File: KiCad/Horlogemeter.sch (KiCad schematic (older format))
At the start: 52 parts, among them J1 Serial header, J10 External LED, J2 AVR-ISP-6, J3 Piezo microphone, J4 12v input, J5 Headphones, J6 Gain pot 10k, J7 RTC connector board, J8 I2c display connector, J9 I2c spare, Q1 BC327, U1 ATmega328P-PU, U2 TL072, U3 OPA37GP, U4 L7805, Y1 16Mhz

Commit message: Schema checked, netlist created
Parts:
- removed C11: 10u, Capacitor_THT:CP_Radial_D5.0mm_P2.50mm, symbol Device:CP
- removed C2: 100n, Capacitor_THT:C_Disc_D3.4mm_W2.1mm_P2.50mm, symbol Device:C
- removed R4, R5: 3k3, Resistor_THT:R_Axial_DIN0207_L6.3mm_D2.5mm_P7.62mm_Horizontal, symbol Device:R
- C15: renamed from C17; value 0,01u -> 0,1u
- renumbered C12 to C10, C13 to C11, C14 to C12, C15 to C13, C16 to C14, C18 to C16, C19 to C17, C3 to C2, C4 to C3, C5 to C4, C6 to C5, C7 to C6, C8 to C7, C9 to C8, C10 to C9, J9 to J10, J10 to J8, J8 to J9, R12 to R10, R13 to R11, R14 to R12, R6 to R4, R7 to R5, R8 to R6, R9 to R7, R10 to R8, R11 to R9
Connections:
- net at U1.5 (PD3): now also J7.5 (Pin_5)
- no-connect marks 15 -> 14

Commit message: PCB v1.1 created
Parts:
- J2: footprint Connector_PinSocket_2.54mm:PinSocket_2x03_P2.54mm_Vertical -> Connector_PinHeader_2.54mm:PinHeader_2x03_P2.54mm_Vertical
- J3, J4, J5, J8: footprint (none) -> TerminalBlock:TerminalBlock_bornier-2_P5.08mm
- J6: footprint (none) -> TerminalBlock:TerminalBlock_bornier-3_P5.08mm
- Q1: footprint Package_TO_SOT_THT:TO-92_Inline -> Package_TO_SOT_THT:TO-92_Inline_Wide
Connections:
- net GND: now also J5.1 (Pin_1); no longer J5.2 (Pin_2)
- net at C14.2: now also J5.2 (Pin_2); no longer J5.1 (Pin_1)
- no-connect marks 14 -> 15
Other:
- moved on the sheet: J5
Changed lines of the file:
@@
 Title "Horlogemeter"
 Date "2021-01-02"
-Rev "1.0"
+Rev "1.1"
 Comp "Jeroen Venema"
 Comment1 ""
@@
 F 0 "J2" V 1783 1000 50  0000 C CNN
 F 1 "AVR-ISP-6" V 1874 1000 50  0000 C CNN
-F 2 "Connector_PinSocket_2.54mm:PinSocket_2x03_P2.54mm_Vertical" V 2000 1000 50  0001 C CNN
+F 2 "Connector_PinHeader_2.54mm:PinHeader_2x03_P2.54mm_Vertical" V 2000 1000 50  0001 C CNN
 F 3 " ~" H 975 400 50  0001 C CNN
 	1    2250 950
@@
 F 0 "Q1" V 9435 4750 50  0000 C CNN
 F 1 "BC327" V 9526 4750 50  0000 C CNN
-F 2 "Package_TO_SOT_THT:TO-92_Inline" H 9400 4675 50  0001 L CIN
+F 2 "Package_TO_SOT_THT:TO-92_Inline_Wide" H 9400 4675 50  0001 L CIN
 F 3 "http://www.onsemi.com/pub_link/Collateral/BC327-D.PDF" H 9200 4750 50  0001 L CNN
 	1    9200 4750
@@
 	6650 5150 6850 5150
 Wire Wire Line
-	5350 6300 6350 6300
-Wire Wire Line
 	6850 5850 6850 6300
 Connection ~ 6850 6300
@@
 	0    1    1    0
 $EndComp
-Wire Wire Line
-	6200 5700 6400 5700
-Wire Wire Line
-	6200 5600 6350 5600
-Wire Wire Line
-	6350 5600 6350 6300
-Connection ~ 6350 6300
-Wire Wire Line
-	6350 6300 6850 6300
 $Comp
 L Device:R R1
@@
 F 0 "J4" H 4618 725 50  0000 C CNN
 F 1 "12v input" H 4618 816 50  0000 C CNN
-F 2 "" H 4700 1050 50  0001 C CNN
+F 2 "TerminalBlock:TerminalBlock_bornier-2_P5.08mm" H 4700 1050 50  0001 C CNN
 F 3 "~" H 4700 1050 50  0001 C CNN
 	1    4700 1050
@@
 F 0 "J3" H 2268 4925 50  0000 C CNN
 F 1 "Piezo microphone" H 2500 5400 50  0000 C CNN
-F 2 "" H 2350 5250 50  0001 C CNN
+F 2 "TerminalBlock:TerminalBlock_bornier-2_P5.08mm" H 2350 5250 50  0001 C CNN
 F 3 "~" H 2350 5250 50  0001 C CNN
 	1    2350 5250
@@
 L Connector:Screw_Terminal_01x02 J5
 U 1 1 6005D483
-P 6000 5700
-F 0 "J5" H 5918 5375 50  0000 C CNN
-F 1 "Headphones" H 5918 5466 50  0000 C CNN
-F 2 "" H 6000 5700 50  0001 C CNN
-F 3 "~" H 6000 5700 50  0001 C CNN
-	1    6000 5700
+P 6000 5800
+F 0 "J5" H 5918 5475 50  0000 C CNN
+F 1 "Headphones" H 5918 5566 50  0000 C CNN
+F 2 "TerminalBlock:TerminalBlock_bornier-2_P5.08mm" H 6000 5800 50  0001 C CNN
+F 3 "~" H 6000 5800 50  0001 C CNN
+	1    6000 5800
 	-1   0    0    1
 $EndComp
@@
 F 0 "J6" H 6768 4225 50  0000 C CNN
 F 1 "Gain pot 10k" H 6850 4750 50  0000 C CNN
-F 2 "" H 6850 4550 50  0001 C CNN
+F 2 "TerminalBlock:TerminalBlock_bornier-3_P5.08mm" H 6850 4550 50  0001 C CNN
 F 3 "~" H 6850 4550 50  0001 C CNN
 	1    6850 4550
@@
 F 0 "J8" H 8868 5625 50  0000 C CNN
 F 1 "External LED" H 8868 5716 50  0000 C CNN
-F 2 "" H 8950 5950 50  0001 C CNN
+F 2 "TerminalBlock:TerminalBlock_bornier-2_P5.08mm" H 8950 5950 50  0001 C CNN
 F 3 "~" H 8950 5950 50  0001 C CNN
 	1    8950 5950
@@
 	950  7500 1900 7500
 NoConn ~ 4050 4900
+Wire Wire Line
+	5350 6300 6200 6300
+Wire Wire Line
+	6200 5700 6400 5700
+Wire Wire Line
+	6200 5800 6200 6300
+Connection ~ 6200 6300
+Wire Wire Line
+	6200 6300 6850 6300
+NoConn ~ 1700 4100
 $EndSCHEMATC

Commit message: Created new PCB with Gerbers
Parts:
- U4: footprint Package_TO_SOT_THT:TO-220-3_Vertical -> Package_TO_SOT_THT:TO-220-3_Horizontal_TabDown
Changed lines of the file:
@@
 F 0 "U4" H 6450 1192 50  0000 C CNN
 F 1 "L7805" H 6450 1101 50  0000 C CNN
-F 2 "Package_TO_SOT_THT:TO-220-3_Vertical" H 6475 800 50  0001 L CIN
+F 2 "Package_TO_SOT_THT:TO-220-3_Horizontal_TabDown" H 6475 800 50  0001 L CIN
 F 3 "http://www.st.com/content/ccc/resource/technical/document/datasheet/41/4f/b3/b0/12/d4/47/88/CD00000444.pdf/files/CD00000444.pdf/jcr:content/translations/en.CD00000444.pdf" H 6450 900 50  0001 C CNN
 	1    6450 950

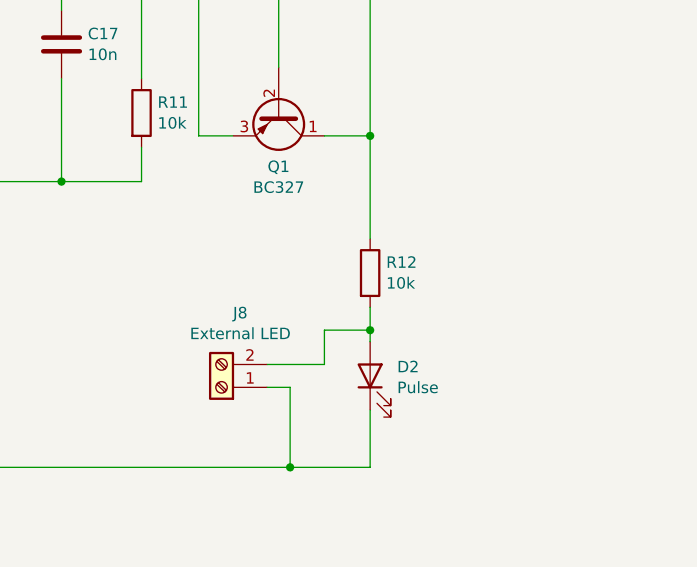
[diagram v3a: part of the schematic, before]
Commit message: R12 to 1K / C16 to ceramic
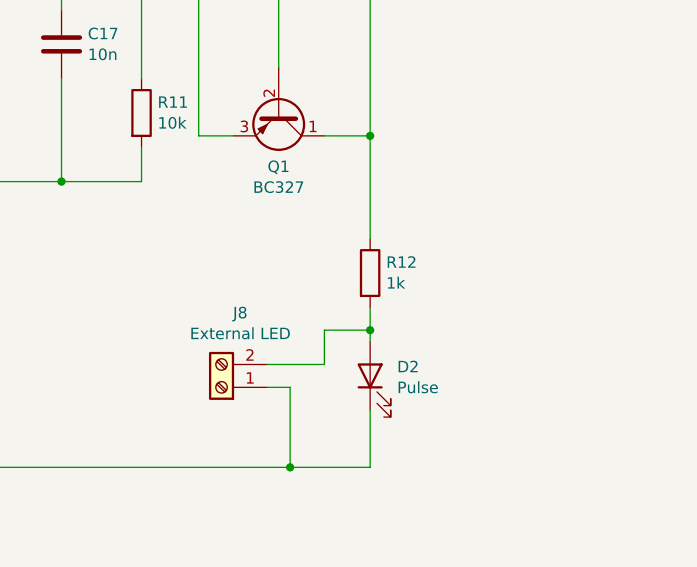
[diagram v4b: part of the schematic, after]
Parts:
- C16: footprint Capacitor_THT:CP_Radial_D5.0mm_P2.50mm -> Capacitor_THT:C_Disc_D3.4mm_W2.1mm_P2.50mm
- R12: value 10k -> 1k
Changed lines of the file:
@@
 Sheet 1 1
 Title "Horlogemeter"
-Date "2021-01-02"
-Rev "1.1"
+Date "2021-01-25"
+Rev "1.2"
 Comp "Jeroen Venema"
 Comment1 ""
@@
 F 0 "C16" V 7348 4450 50  0000 C CNN
 F 1 "1u" V 7439 4450 50  0000 C CNN
-F 2 "Capacitor_THT:CP_Radial_D5.0mm_P2.50mm" H 7638 4300 50  0001 C CNN
+F 2 "Capacitor_THT:C_Disc_D3.4mm_W2.1mm_P2.50mm" H 7638 4300 50  0001 C CNN
 F 3 "~" H 7600 4450 50  0001 C CNN
 	1    7600 4450
@@
 P 9600 5450
 F 0 "R12" H 9670 5496 50  0000 L CNN
-F 1 "10k" H 9670 5405 50  0000 L CNN
+F 1 "1k" H 9670 5405 50  0000 L CNN
 F 2 "Resistor_THT:R_Axial_DIN0207_L6.3mm_D2.5mm_P7.62mm_Horizontal" V 9530 5450 50  0001 C CNN
 F 3 "~" H 9600 5450 50  0001 C CNN
